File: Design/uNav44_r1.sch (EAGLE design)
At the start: 36 parts, among them IC1 DSPIC33FJ128MC, IC2 24LC024, Q1 10MHz

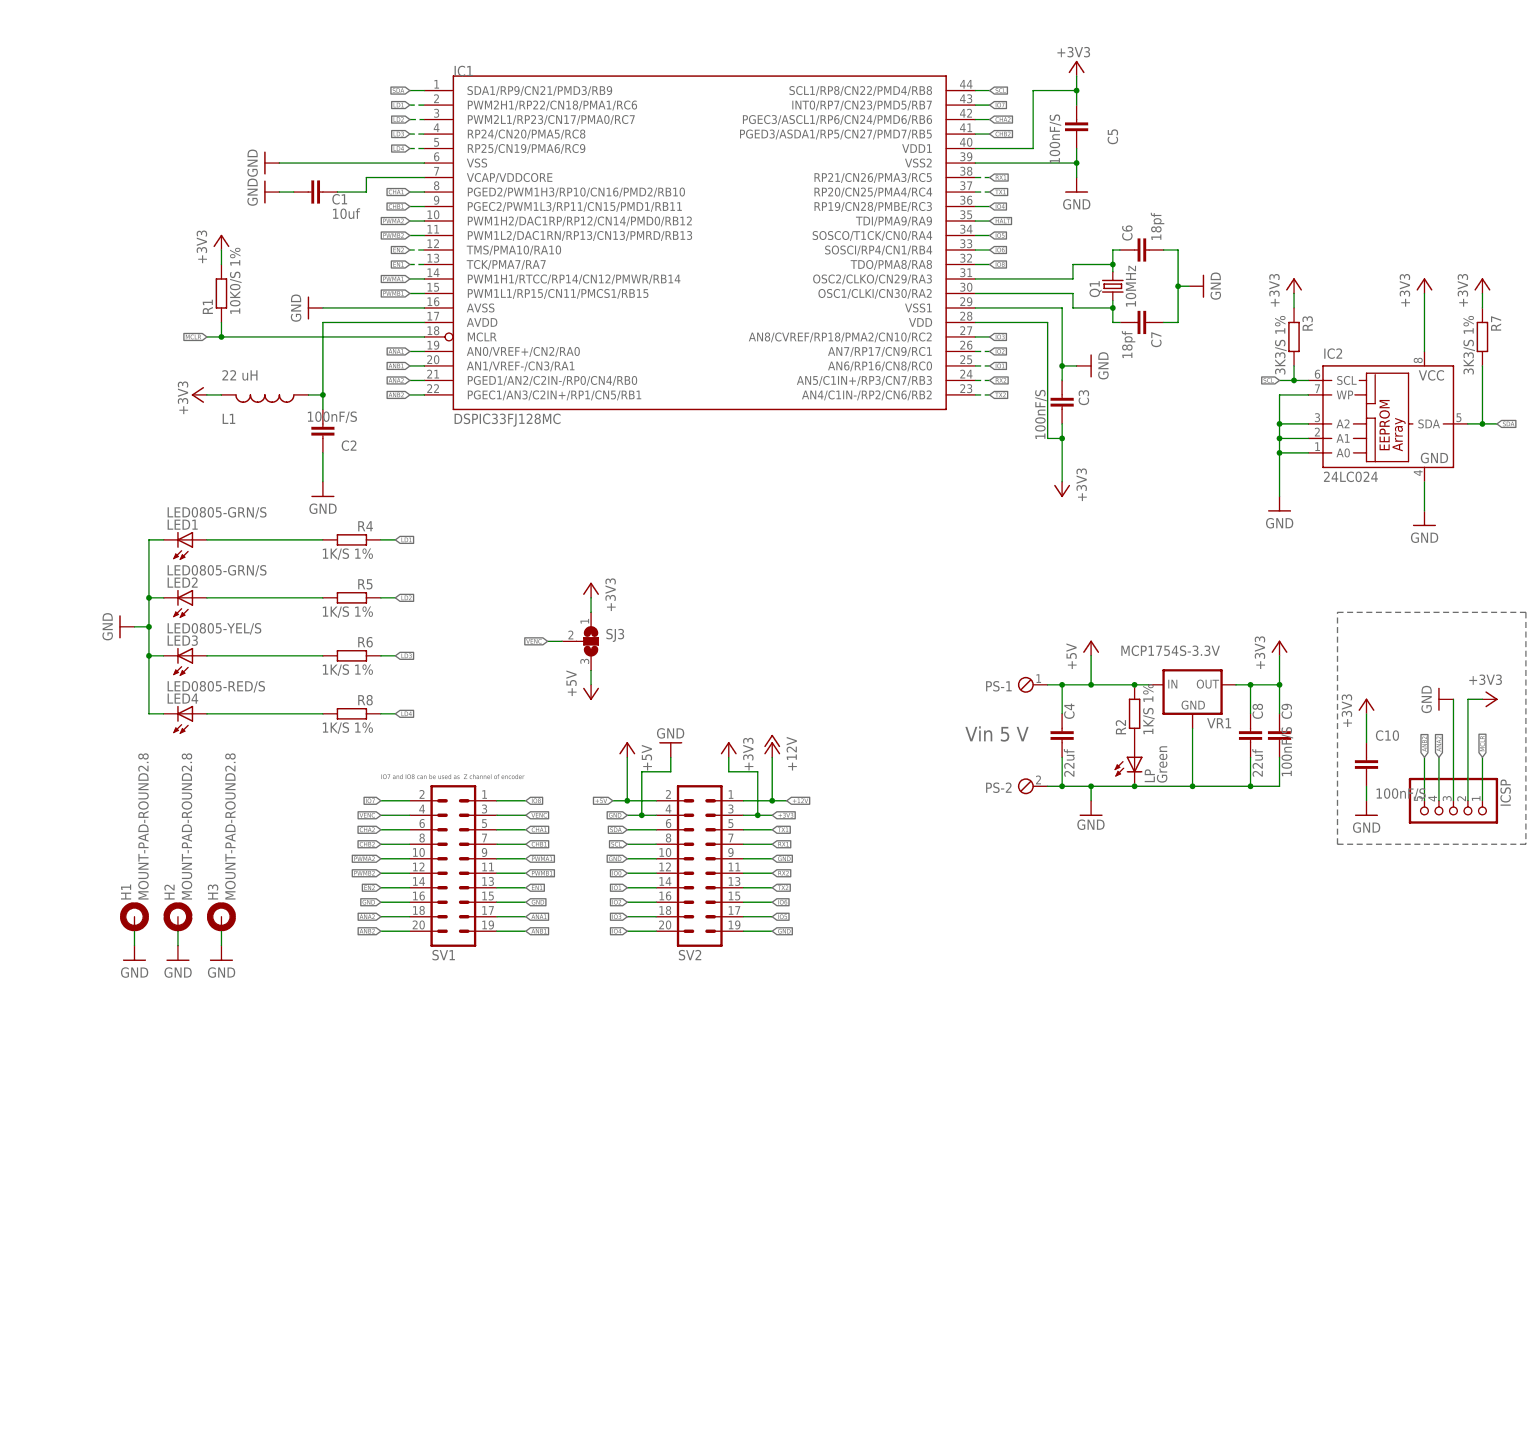
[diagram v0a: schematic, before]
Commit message: Add 5 and 3.3V regulator / @katodo you must verify
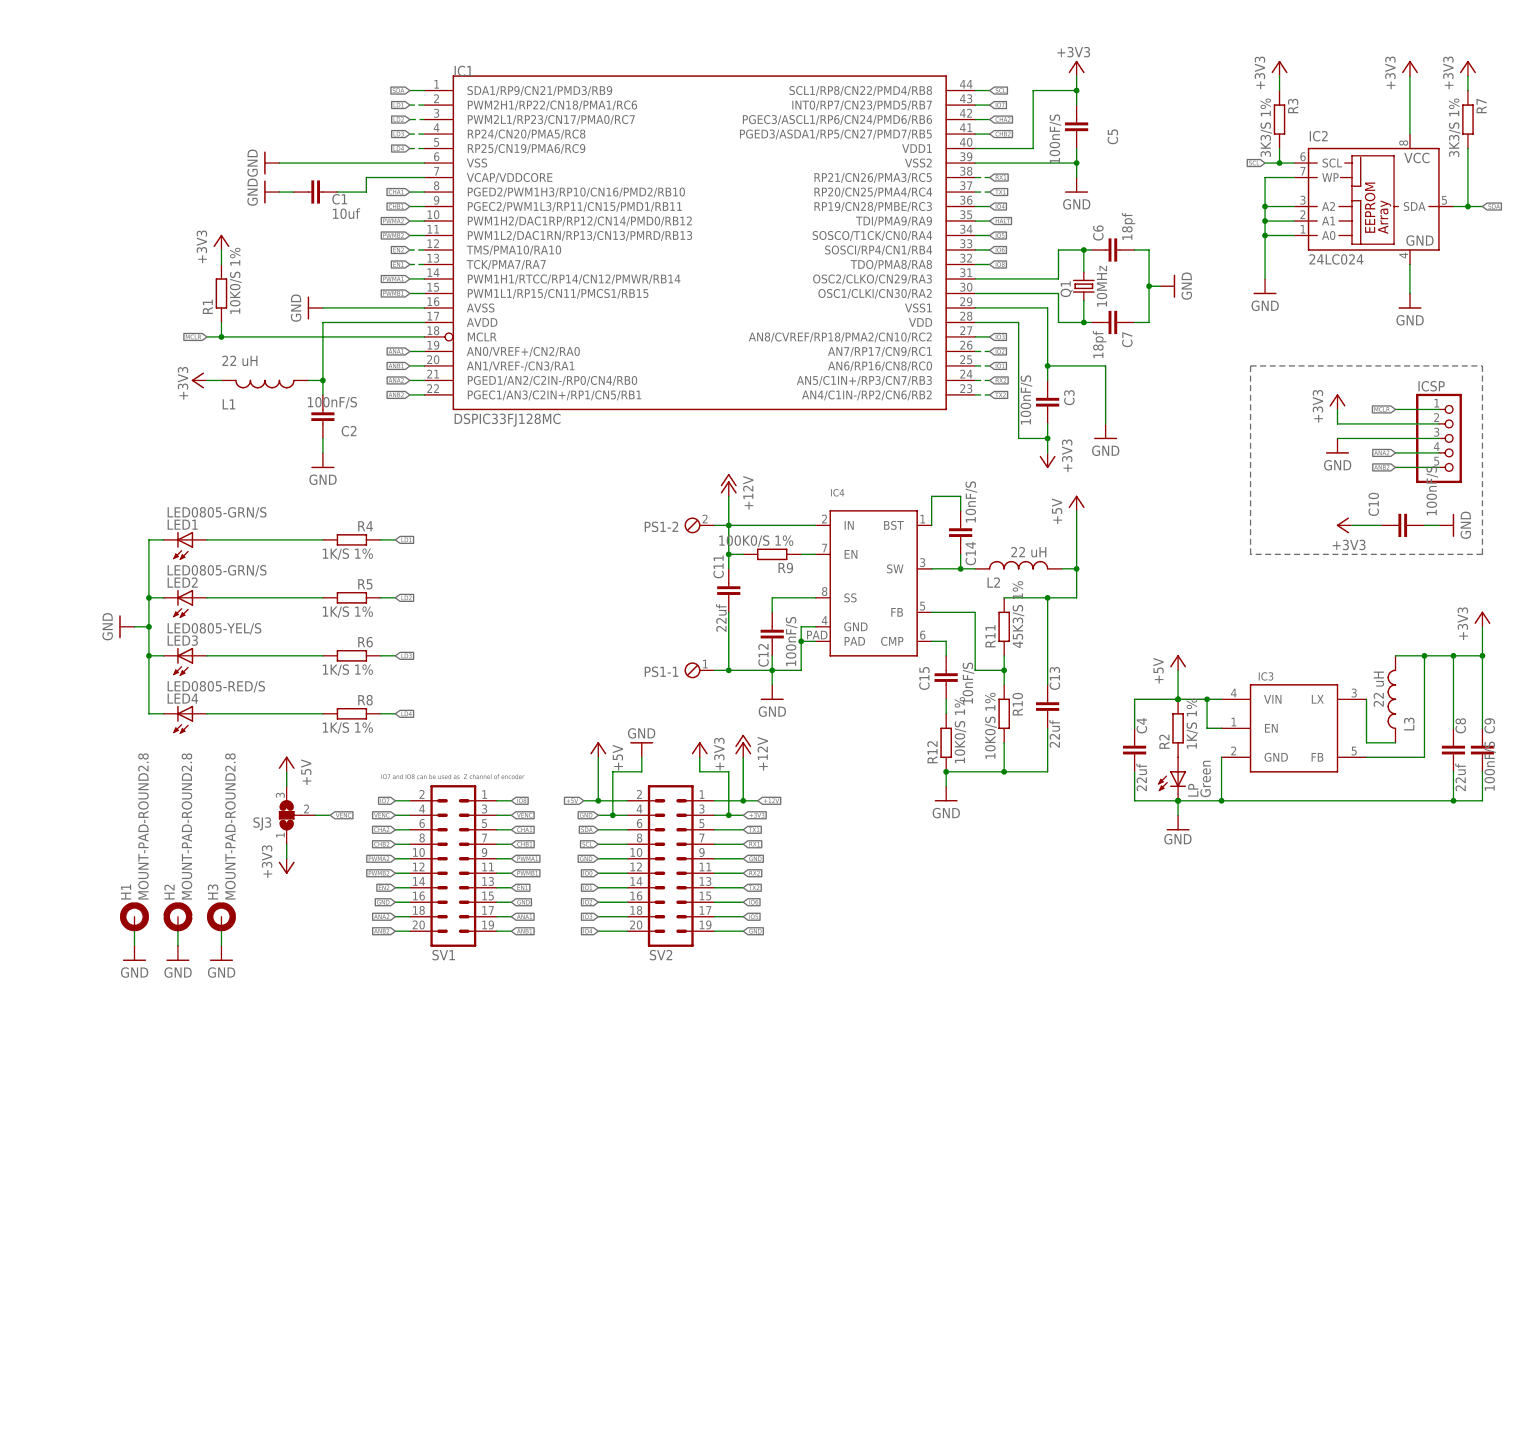
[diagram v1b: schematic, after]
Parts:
- removed PS: (no value), Personale:MPT2
- removed VR1: MCP1754S-3.3V, Personale:MCP1754S
- added C11, C13: 22uf, rcl:C-EUC1206
- added C12: 100nF/S, rcl:C-EUC0603
- added C14, C15: 10nF/S, rcl:C-EUC0603
- added IC3: (no value), OfficineRobotiche:AP3417CSOT-23-5
- added IC4: (no value), OfficineRobotiche:AP6503SP-13'SO-8EP'
- added L2, L3: 22 uH, SparkFun-Passives:INDUCTOR0805
- added PS1: (no value), Personale:MPT2
- added R10, R12: 10K0/S 1%, rcl:R-EU_R0603
- added R11: 45K3/S 1%, rcl:R-EU_R0603
- added R9: 100K0/S 1%, rcl:R-EU_R0603
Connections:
- new net N$1: IC3.LX, L3.1
- new net N$15: C14.2, IC4.SW, L2.1
- new net N$16: C15.1, IC4.CMP
- new net N$17: C15.2, R12.2
- new net N$4: C14.1, IC4.BST
- new net N$6: IC4.EN, R9.1
- new net N$8: C12.1, IC4.SS
- new net N$9: IC4.FB, R10.1, R11.1
- net +12V: now also C11.1, IC4.IN, PS1-2.1, R9.2
- net +3V3: now also IC3.FB, L3.2; no longer VR1.OUT
- net +5V: now also C13.1, IC3.EN, IC3.VIN, L2.2, R11.2; no longer PS-1.1, VR1.IN
- net GND: now also C11.2, C12.2, C13.2, IC3.GND, IC4.GND, IC4.PAD, PS1-1.1, R10.2, R12.1; no longer PS-2.1, VR1.GND
- net VENC: now also SJ3.2
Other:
- note removed: "Vin 5 V"
- moved on the sheet: C10, C2, C3, C4, C6, C7, C8, C9, IC2, ICSP, L1, LP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

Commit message: Changed some component package to optimize space.
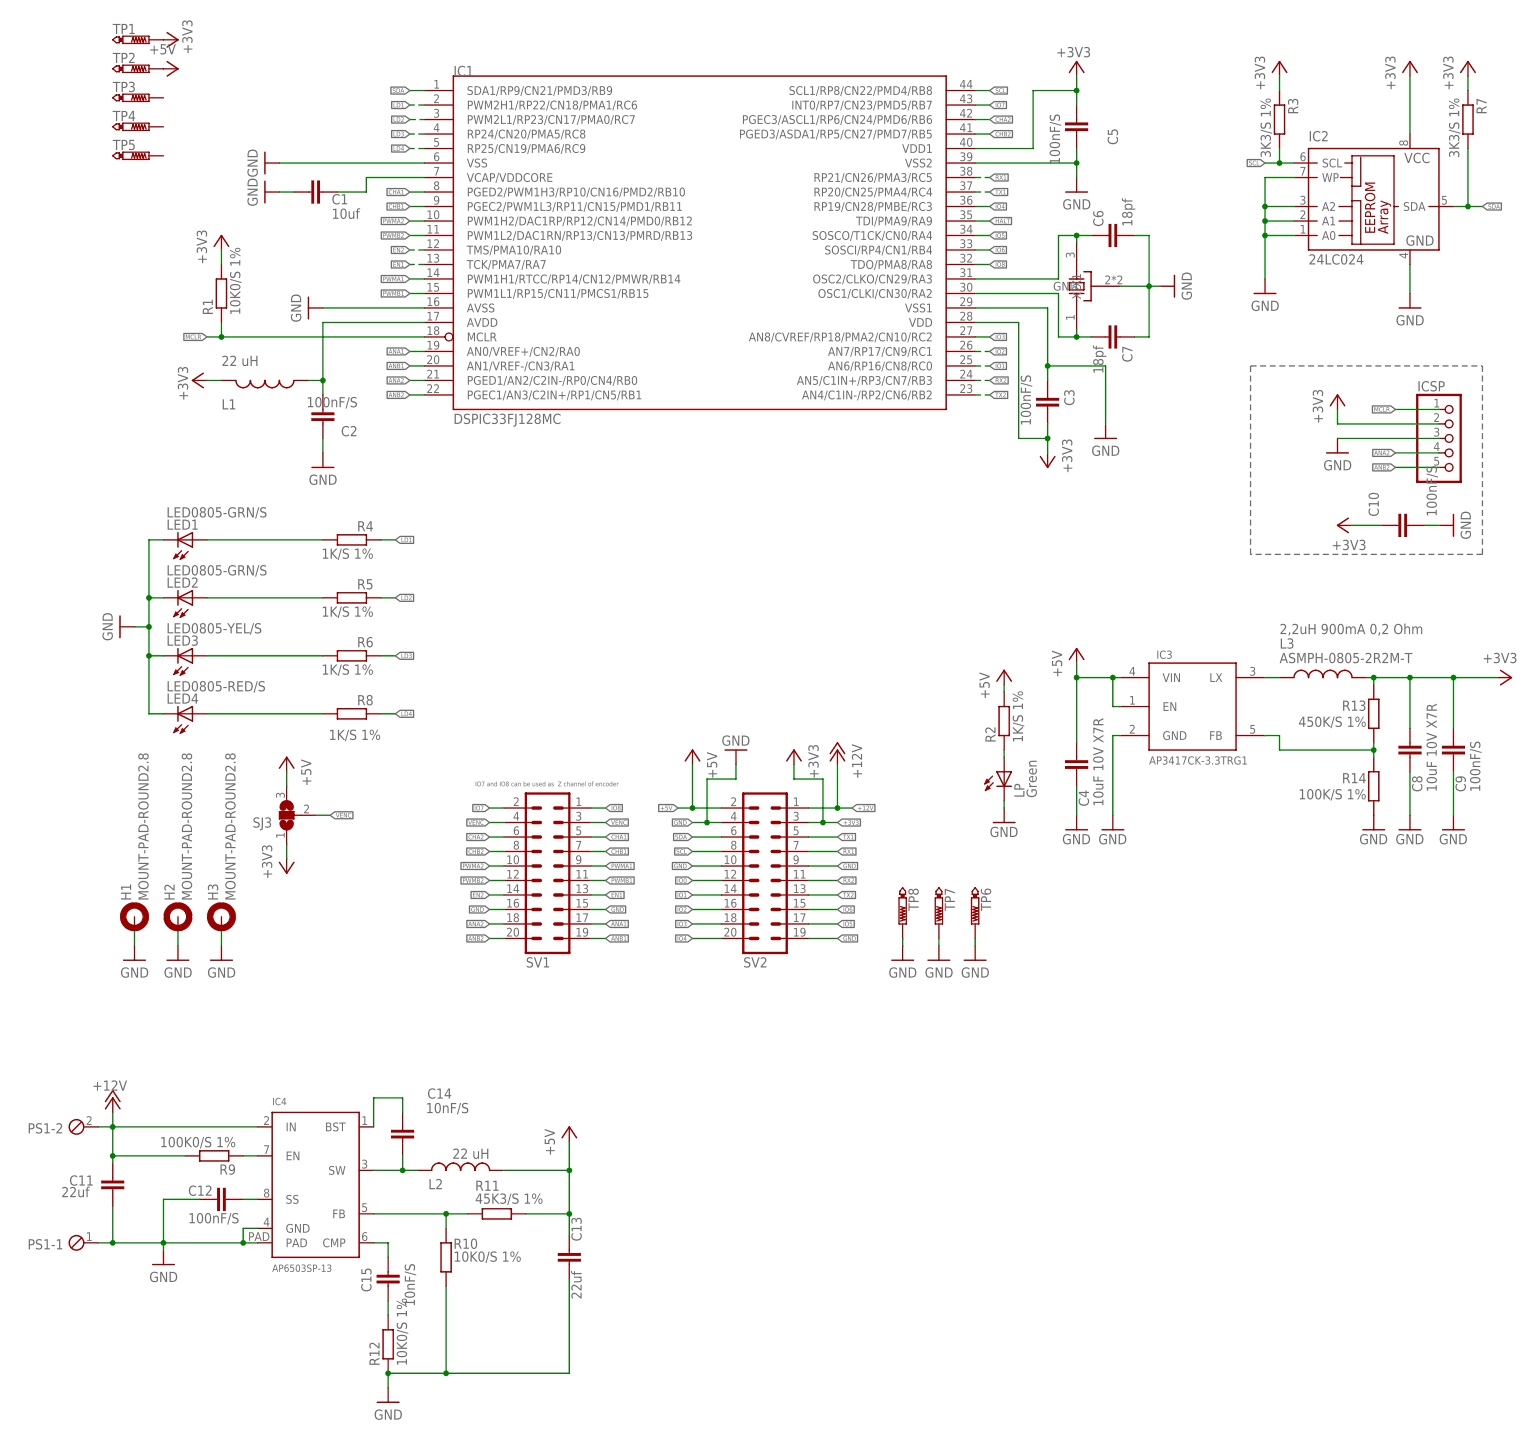
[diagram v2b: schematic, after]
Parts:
- removed Q1: 10MHz, crystal:CRYSTALHC49U-V
- added R13: 450K/S 1%, rcl:R-EU_R0603
- added R14: 100K/S 1%, rcl:R-EU_R0603
- added TP1, TP2, TP3, TP4, TP5: PTR1TP07R, testpad:PTR1TP07R
- added TP6, TP7, TP8: PTR1PAD1-13, testpad:PTR1PAD1-13
- added U$1: CTS_32X25_SMD, cts_crystal:CTS_32X25_SMD
- C4, C8: value 22uf -> 10uF 10V X7R; device rcl:C-EUC1206 -> rcl:C-EUC0805
- IC3: value (none) -> AP3417CK-3.3TRG1
- IC4: value (none) -> AP6503SP-13
- L3: value 22 uH -> ASMPH-0805-2R2M-T
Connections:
- new net N$7: IC3.FB, R13.1, R14.2
- net +3V3: now also R13.2, TP1.TP; no longer IC3.FB
- net +5V: now also TP2.TP
- net GND: now also R14.1, TP6.TP, TP7.TP, TP8.TP, U$1.GND
- net N$2: now also U$1.X1; no longer Q1.1
- net N$3: now also U$1.X2; no longer Q1.2
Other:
- note added: "2,2uH 900mA 0,2 Ohm"
- moved on the sheet: C11, C12, C13, C14, C15, C4, C6, C7, C8, C9, IC3, IC4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

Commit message: Scheme update with Operational Amplifier and switching supply
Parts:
- removed PS1: (no value), Personale:MPT2
- removed TP6, TP7, TP8: PTR1PAD1-13, testpad:PTR1PAD1-13
- added C16, C17: 100nF/S, rcl:C-EUC0603
- added JMP1, JMP2, JMP3, JMP4: 0R-JUMPC, jump-0r-smd:0R-JUMPC
- added JP1: M02LOCK, SparkFun-Connectors:M02LOCK
- added R15, R16: 10K0/S 1%, rcl:R-EU_R0603
- added U1, U2, U3, U4: MCP6G01T-E/OT, OfficineRobotiche:MCP6G01T-E/OT
- C11: value 22uf -> 22uF 35V 20% JB 1206
- C12: value 100nF/S -> 100nF/S2
- C15: value 10nF/S -> 10nF/S2
- L2: value 22 uH -> 10uH_520mA; device SparkFun-Passives:INDUCTOR0805 -> SparkFun-Passives:INDUCTOR1210
- R9: value 100K0/S 1% -> 100K0/S2 1%
- U$1: value CTS_32X25_SMD -> (none); device cts_crystal:CTS_32X25_SMD -> OfficineRobotiche:CTS_32X25_SMD
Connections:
- new net ANA2/PGD: IC1.PGED1/AN2/C2IN-/RP0/CN4/RB0, ICSP.4, R15.1
- new net ANB2/PGC: IC1.PGEC1/AN3/C2IN+/RP1/CN5/RB1, ICSP.5, R16.1
- new net IN_A1: SV1.17, U3.VIN+
- new net IN_B1: SV1.19, U4.VIN+
- new net N$11: JMP1-0R.2, U1.GSEL
- new net N$18: JMP2-0R.2, U2.GSEL
- new net N$19: JMP3-0R.2, U3.GSEL
- new net N$20: JMP4-0R.2, U4.GSEL
- new net N$21: R15.2, U1.VOUT
- new net N$22: R16.2, U2.VOUT
- net +12V: now also JP1.2; no longer PS1-2.1
- net +3V3: now also C16.1, C17.1, JMP1-0R.1, JMP2-0R.1, JMP3-0R.1, JMP4-0R.1, U1.VDD, U2.VDD, U3.VDD, U4.VDD
- net ANA1: now also U3.VOUT; no longer SV1.17
- net ANA2: now also U1.VIN+; no longer IC1.PGED1/AN2/C2IN-/RP0/CN4/RB0, ICSP.4
- net ANB1: now also U4.VOUT; no longer SV1.19
- net ANB2: now also U2.VIN+; no longer IC1.PGEC1/AN3/C2IN+/RP1/CN5/RB1, ICSP.5
- net GND: now also C16.2, C17.2, JMP1-0R.3, JMP2-0R.3, JMP3-0R.3, JMP4-0R.3, JP1.1, U1.VSS, U2.VSS, U3.VSS, U4.VSS; no longer PS1-1.1, TP6.TP, TP7.TP, TP8.TP
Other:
- note added: "3,3V Power Supply"
- note added: "5V Power Supply"
- note added: "Encoder voltage selection"
- note added: "V Input : 5V V Output : 3,3V Max output current : 500mA"
- note added: "V Input : 6-23V V Output : 5V Max output current : 600mA"

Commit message: Work in progress... update image of layout
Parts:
- added C18, C19: 100nF/S, rcl:C-EUC0603
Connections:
- net +3V3: now also C18.1, C19.1
- net GND: now also C18.2, C19.2
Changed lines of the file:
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@@
 <part name="GND19" library="supply1" deviceset="GND" device=""/>
 <part name="GND21" library="supply1" deviceset="GND" device=""/>
+<part name="C18" library="rcl" deviceset="C-EU" device="C0603" value="100nF/S"/>
+<part name="C19" library="rcl" deviceset="C-EU" device="C0603" value="100nF/S"/>
+<part name="GND22" library="supply1" deviceset="GND" device=""/>
+<part name="GND32" library="supply1" deviceset="GND" device=""/>
+<part name="+3V13" library="supply1" deviceset="+3V3" device=""/>
+<part name="+3V14" library="supply1" deviceset="+3V3" device=""/>
 </parts>
 <sheets>
@@
 <attribute name="VALUE" x="81.28" y="55.88" size="1.27" layer="96" rot="R180"/>
 </instance>
+<instance part="C18" gate="G$1" x="85.09" y="67.31" smashed="yes">
+<attribute name="NAME" x="83.82" y="59.69" size="1.778" layer="95" rot="R90"/>
+</instance>
+<instance part="C19" gate="G$1" x="90.17" y="67.31" smashed="yes">
+<attribute name="NAME" x="88.9" y="59.69" size="1.778" layer="95" rot="R90"/>
+</instance>
+<instance part="GND22" gate="1" x="85.09" y="59.69" smashed="yes">
+<attribute name="VALUE" x="87.63" y="58.42" size="1.27" layer="96" rot="R180"/>
+</instance>
+<instance part="GND32" gate="1" x="90.17" y="59.69" smashed="yes">
+<attribute name="VALUE" x="92.71" y="58.42" size="1.27" layer="96" rot="R180"/>
+</instance>
+<instance part="+3V13" gate="G$1" x="85.09" y="72.39" smashed="yes" rot="MR0">
+<attribute name="VALUE" x="87.63" y="73.66" size="1.27" layer="96" rot="MR0"/>
+</instance>
+<instance part="+3V14" gate="G$1" x="90.17" y="72.39" smashed="yes" rot="MR0">
+<attribute name="VALUE" x="92.71" y="73.66" size="1.27" layer="96" rot="MR0"/>
+</instance>
 </instances>
 <busses>
@@
 <pinref part="+3V12" gate="G$1" pin="+3V3"/>
 <wire x1="78.74" y1="69.85" x2="78.74" y2="72.39" width="0.1524" layer="91"/>
+</segment>
+<segment>
+<pinref part="C18" gate="G$1" pin="1"/>
+<pinref part="+3V13" gate="G$1" pin="+3V3"/>
+</segment>
+<segment>
+<pinref part="C19" gate="G$1" pin="1"/>
+<pinref part="+3V14" gate="G$1" pin="+3V3"/>
 </segment>
 </net>
@@
 <wire x1="78.74" y1="59.69" x2="78.74" y2="62.23" width="0.1524" layer="91"/>
 </segment>
-</net>
+<segment>
+<pinref part="C18" gate="G$1" pin="2"/>
+<pinref part="GND22" gate="1" pin="GND"/>
+</segment>
+<segment>
+<pinref part="C19" gate="G$1" pin="2"/>
+<pinref part="GND32" gate="1" pin="GND"/>
+</segment>
+</net>
